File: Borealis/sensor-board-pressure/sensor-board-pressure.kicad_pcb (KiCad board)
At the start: 2 copper layers, 3 parts, among them J1 Conn_01x06_Pin, J2 Conn_01x08_Pin (BMP390)

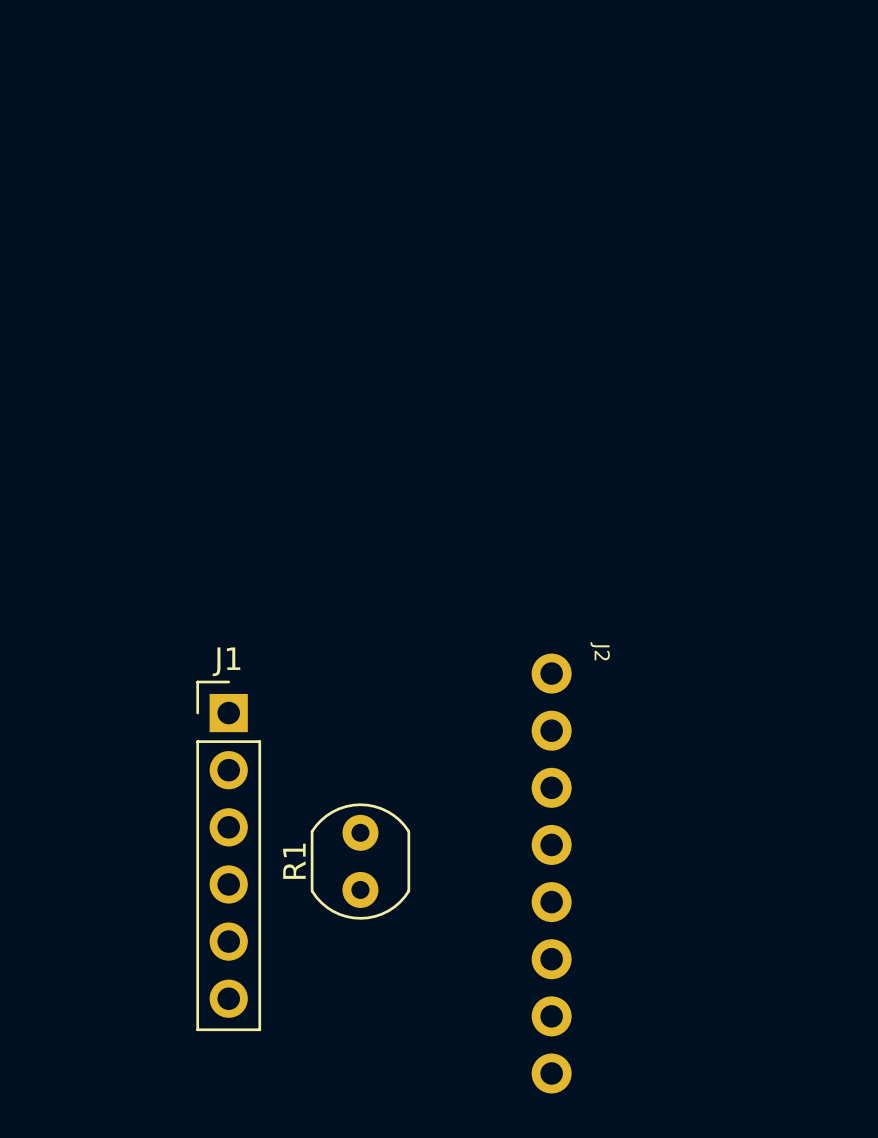
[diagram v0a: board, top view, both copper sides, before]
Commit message: Added barometric sensor board
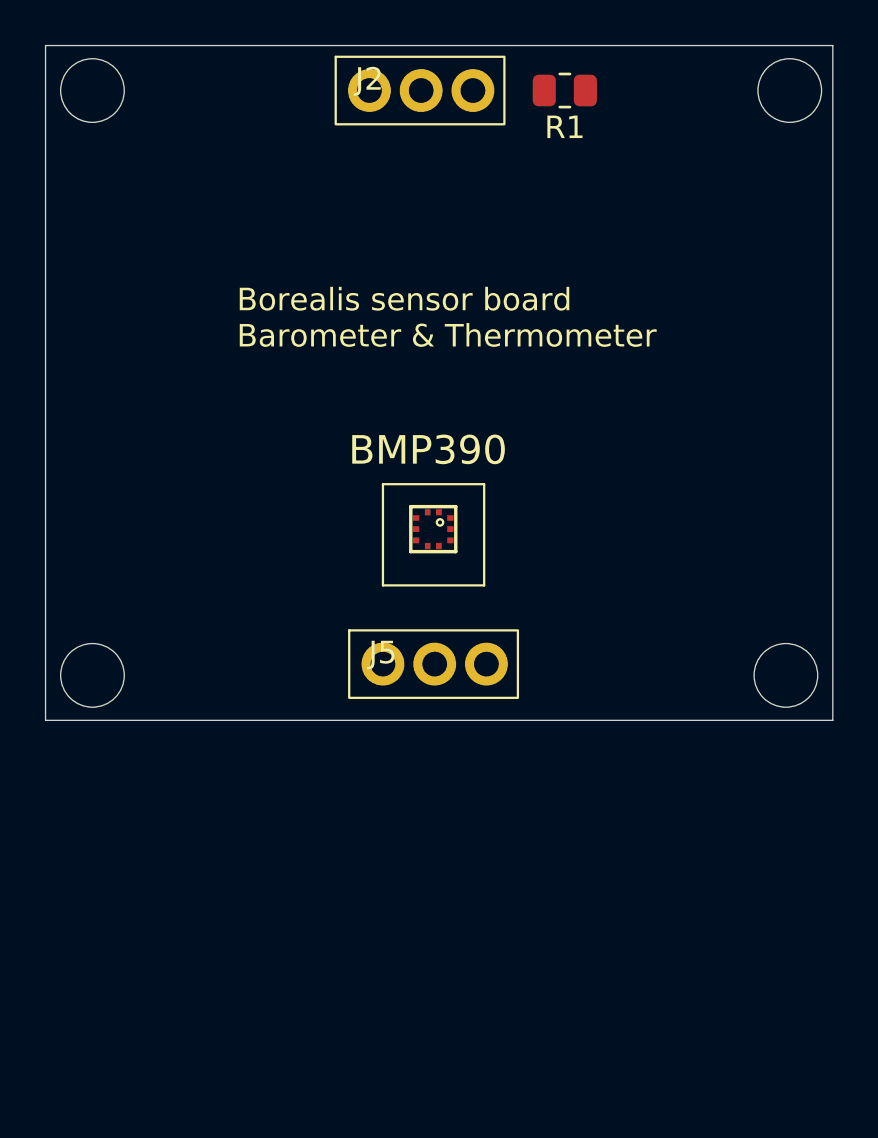
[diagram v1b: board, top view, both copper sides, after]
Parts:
- removed J1: Conn_01x06_Pin, Connector_PinHeader_2.54mm:PinHeader_1x06_P2.54mm_Vertical
- added BMP390: ~, Adafruit BMP390:BMP388, F.Cu at (117.2, 71.5)
- added J5: Conn_01x03_Pin (power connection to main board), batteryholder:1x03 2.3 pitch, F.Cu at (115.0, 77.5)
- J2: value Conn_01x08_Pin (BMP390) -> Conn_01x03_Pin (data connection to main board); footprint Adafruit BMP390:1X08_ROUND_70 -> batteryholder:1x03 2.3 pitch
- R1: footprint OptoDevice:R_LDR_4.9x4.2mm_P2.54mm_Vertical -> Resistor_SMD:R_0805_2012Metric
- moved R1 36.7 mm to (123.1, 52.0), turned to 180 degrees
- moved J2 35.7 mm to (114.4, 52.0), turned to 0 degrees
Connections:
- J2 pad 1: +3.3V -> /SCL
- J2 pad 2: unconnected-(J2-Pin_2-Pad2) -> /SDA
- J2 pad 3: GND -> /ADC
- R1 pad 2: Net-(J1-Pin_6) -> /ADC
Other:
- board outline added: 35 x 30 mm
- board text added: "Borealis sensor board Barometer & Thermometer"

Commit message: .
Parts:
- moved J2 44.1 mm to (158.5, 51.2), turned to -90 degrees
- moved J5 38.0 mm to (142.5, 51.2), turned to -90 degrees
- moved BMP390 37.2 mm to (149.8, 53.5), turned to 180 degrees
- moved R1 31.3 mm to (153.5, 59.5), turned to 0 degrees
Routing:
- net /SCL: track 0.00 -> 21.1 mm
- net +3.3V: track 0.00 -> 18.6 mm
- net GND: track 0.00 -> 9.89 mm
- net /SDA: track 0.00 -> 8.00 mm
- net /ADC: track 0.00 -> 5.60 mm
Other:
- board size 35 x 30 mm -> 20 x 20 mm
- board text added: "${REFERENCE}"
- board text added: "Borealis Sensor Board Solar panel"
- board text added: "Conn_01x03_Pin (data connection to main board)"
- board text removed: "Borealis sensor board Barometer & Thermometer"

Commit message: updated
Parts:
- added R2: 10k, Resistor_SMD:R_0805_2012Metric, F.Cu at (66.0, 62.4)
- moved J2 101.1 mm to (57.4, 52.5), turned to 0 degrees
- moved BMP390 89.7 mm to (60.2, 59.8), turned to 0 degrees
- moved R1 87.5 mm to (66.1, 56.5), turned to 90 degrees
- moved J5 86.1 mm to (57.9, 67.5), turned to 0 degrees
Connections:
- BMP390 pad 3: unconnected-(BMP390-VSS-Pad3) -> GND
- BMP390 pad 6: +3.3V -> Net-(BMP390-CSB)
- BMP390 pad 9: unconnected-(BMP390-VSS-Pad9) -> GND
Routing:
- net /SCL: track 21.1 -> 7.45 mm
- net +3.3V: track 18.6 -> 26.1 mm
- net Net-(BMP390-CSB): track 0.00 -> 7.38 mm
- net GND: track 9.89 -> 3.72 mm, vias 0 -> 3
- net /SDA: track 8.00 -> 13.8 mm
- net /ADC: track 5.60 -> 5.07 mm
- added copper zone on B.Cu, net GND
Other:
- outline, holes or cut-outs redrawn
- board text added: "Borealis sensor module pressure sensor"
- board text removed: "${REFERENCE}"
- board text removed: "Borealis Sensor Board Solar panel"

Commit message: Worked on sum stuff
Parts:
- removed J2: Conn_01x03_Pin (data connection to main board), batteryholder:1x03 2.3 pitch
- removed J5: Conn_01x03_Pin (power connection to main board), batteryholder:1x03 2.3 pitch
- added C1: 100nF, Capacitor_SMD:C_0805_2012Metric, F.Cu at (101.9, 58.2)
- added C5: 100nF, Capacitor_SMD:C_0805_2012Metric, F.Cu at (101.9, 61.0)
- added R3: 4.7kOhms, Resistor_SMD:R_0805_2012Metric, F.Cu at (100.5, 67.7)
- added U1: MAGNETIC POGO CONN., batteryholder:MAGNETIC POGO CONN., F.Cu at (110.2, 63.7)
- added U2: MAGNETIC POGO CONN., batteryholder:MAGNETIC POGO CONN., F.Cu at (93.2, 63.7)
- BMP390: moved to B.Cu
- R2: value 10k -> 4.7kOhms
- moved BMP390 41.7 mm to (101.8, 64.2)
- moved R2 37.7 mm to (103.3, 67.8)
- moved R1 32.4 mm to (98.4, 58.9), turned to -90 degrees
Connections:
- BMP390 pad 6: Net-(BMP390-CSB) -> +3.3V
- R1 pad 2: /ADC -> /ID
- R2 pad 1: +3.3V -> /SDA
- R2 pad 2: Net-(BMP390-CSB) -> +3.3V
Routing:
- net +3.3V: track 26.1 -> 0.07 mm
- net /SDA: track 13.8 -> 0.00 mm
- net /SCL: track 7.45 -> 0.00 mm
- net Net-(BMP390-CSB): track 7.38 -> 0.00 mm
- net /ADC: track 5.07 -> 0.00 mm
- net GND: track 3.72 -> 0.00 mm, vias 3 -> 0
- removed copper zone on B.Cu, net GND
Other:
- board size 20 x 20 mm -> 23.6 x 23.5 mm
- board text removed: "Borealis sensor module pressure sensor"
- board text removed: "Conn_01x03_Pin (data connection to main board)"

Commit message: Worked on boards
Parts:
- added H1: MountingHole, MountingHole:MountingHole_2.7mm_M2.5_Pad, F.Cu at (99.3, 74.8)
- moved R1 7.34 mm to (95.4, 65.6), turned to 90 degrees
- moved C5 5.94 mm to (96.1, 62.2), turned to 0 degrees
- moved R2 4.36 mm to (99.4, 69.8), turned to 180 degrees
- moved C1 4.14 mm to (100.7, 62.2)
- moved R3 3.38 mm to (103.2, 65.7)
- moved U1 3.24 mm to (107.8, 65.9)
- moved U2 3.24 mm to (90.8, 65.9)
- moved BMP390 2.83 mm to (99.3, 65.7), turned to 180 degrees
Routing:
- net +3.3V: track 0.07 -> 37.5 mm, vias 0 -> 3
- net /SDA: track 0.00 -> 25.1 mm, vias 0 -> 1
- net /SCL: track 0.00 -> 13.7 mm, vias 0 -> 1
- net /ID: track 0.00 -> 6.50 mm, vias 0 -> 1
- net GND: track 0.00 -> 2.85 mm, vias 0 -> 3
- added copper zone on F.Cu, net GND
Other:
- outline, holes or cut-outs redrawn
- board text added: "Borealis Pressure Sensor"
